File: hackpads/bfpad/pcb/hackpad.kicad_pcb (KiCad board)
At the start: 2 copper layers, 79.8 x 66.7 mm, 34 parts, among them J1 SSD1306, SW1 SW_Push, SW2 SW_Push, SW3 SW_Push, SW4 SW_Push, SW5 SW_Push, SW6 SW_Push, SW7 SW_Push, SW8 SW_Push, SW9 RotaryEncoder_Switch, U1 XIAO-RP2040-DIP

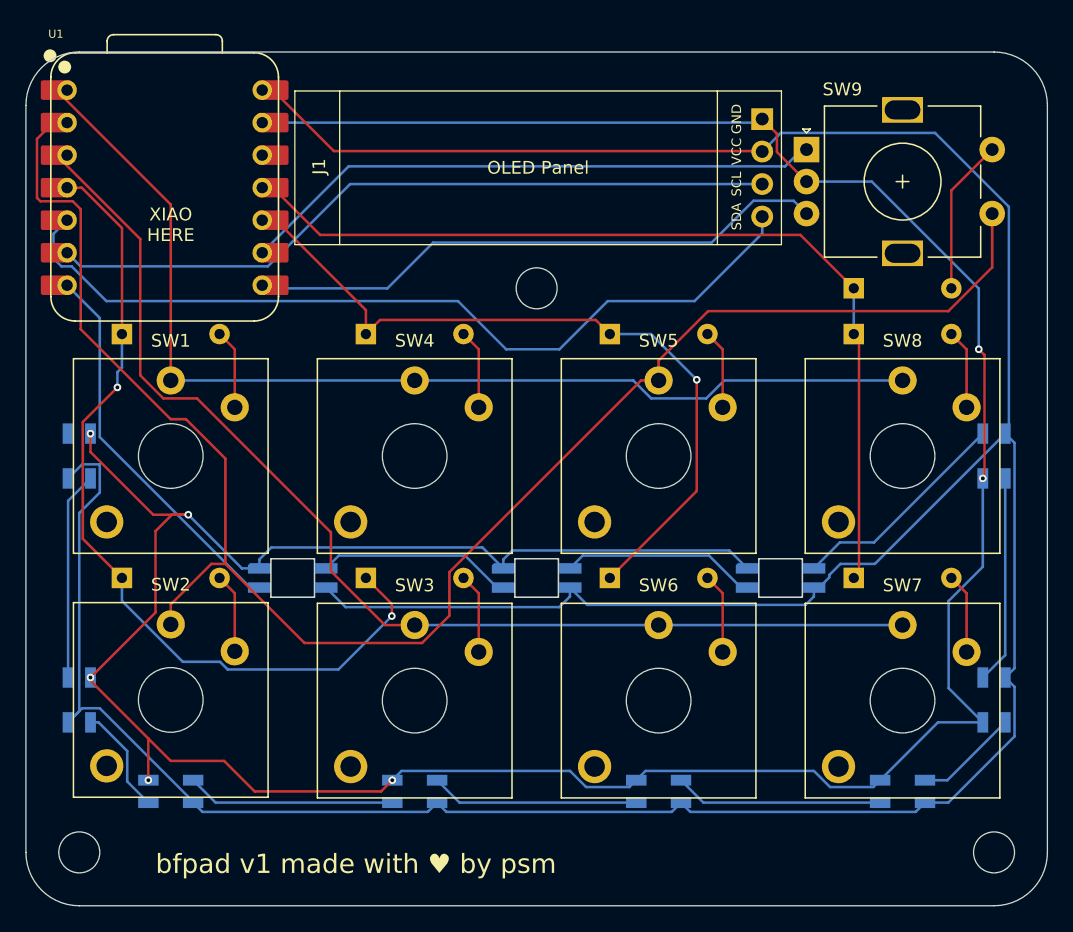
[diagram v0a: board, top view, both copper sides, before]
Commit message: re-route PCB (v2)
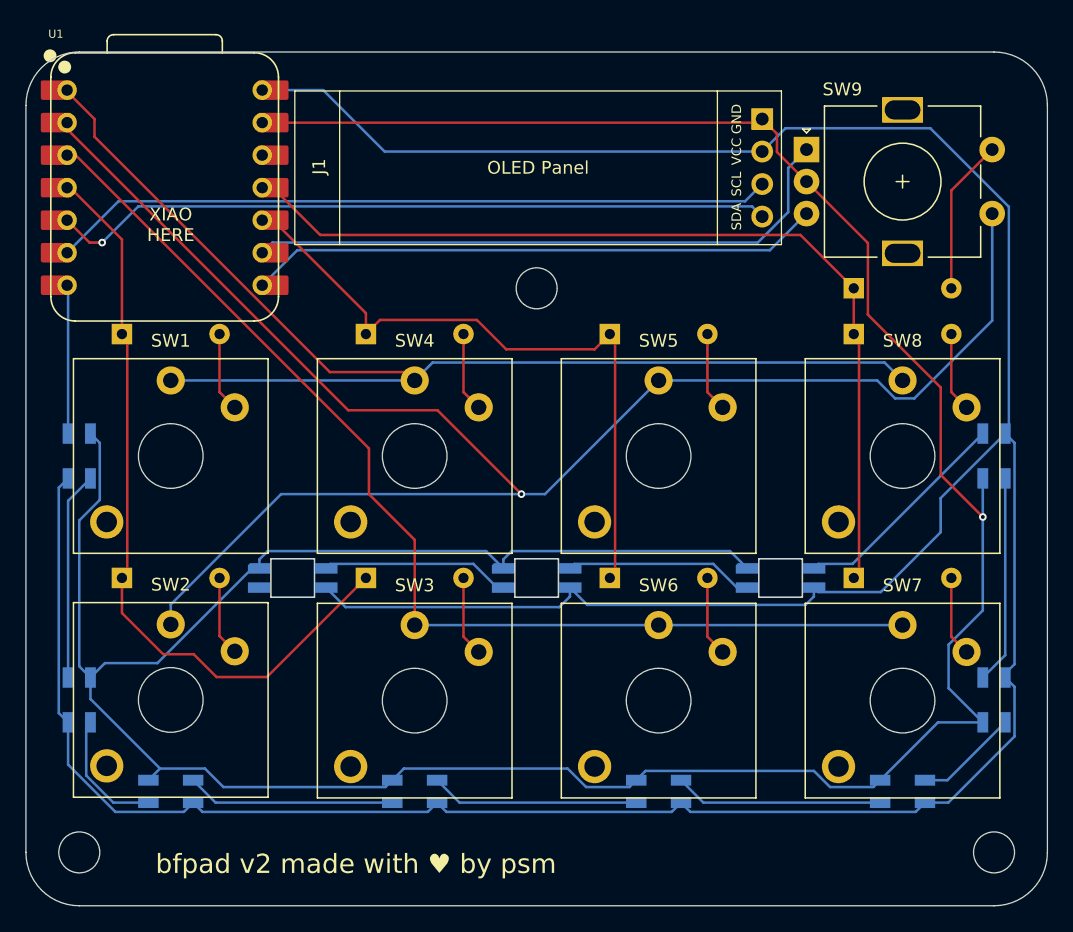
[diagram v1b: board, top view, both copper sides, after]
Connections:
- D19 pad 1: unconnected-(D19-DOUT-Pad1) -> Net-(D19-DOUT)
- D9 pad 3: Net-(D9-DIN) -> unconnected-(D9-DIN-Pad3)
- U1 pad 7: Net-(D9-DIN) -> Net-(D19-DOUT)
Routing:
- net Net-(D9-DIN): track 30.3 -> 0.00 mm
- net Net-(D19-DOUT): track 0.00 -> 11.6 mm
- net COL1: track 84.7 -> 95.7 mm
- net SDA: track 66.8 -> 56.5 mm, vias 0 -> 1
- net ROW2: track 59.6 -> 52.2 mm, vias 1 -> 0
- net ROW1: track 66.1 -> 60.6 mm, vias 2 -> 0
- net COL3: track 89.3 -> 87.3 mm
- net REA: track 46.0 -> 47.9 mm
- net Net-(D17-DOUT): track 8.51 -> 10.0 mm
- net REB: track 45.9 -> 44.8 mm
- net COL2: track 133.2 -> 132.2 mm, vias 0 -> 1
- net SCL: track 57.4 -> 56.5 mm
- net Net-(D10-DIN): track 15.3 -> 14.8 mm
- net Net-(D10-DOUT): track 15.3 -> 14.8 mm
- net GND: track 256.1 -> 255.9 mm, vias 7 -> 1
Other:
- board text added: "bfpad v2 made with ♥︎ by psm"
- board text removed: "bfpad v1 made with ♥︎ by psm"
